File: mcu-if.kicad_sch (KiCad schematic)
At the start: 46 parts, among them J501 MCU_USB, J502 SD_Card, J503 CONN_DISP, J504 RJ45_Amphenol_RJMG1BD3B8K1ANR, SW501 BTN0, SW502 BTN1, SW503 BTN2, SW504 BTN3, U501 KSZ8081RNA

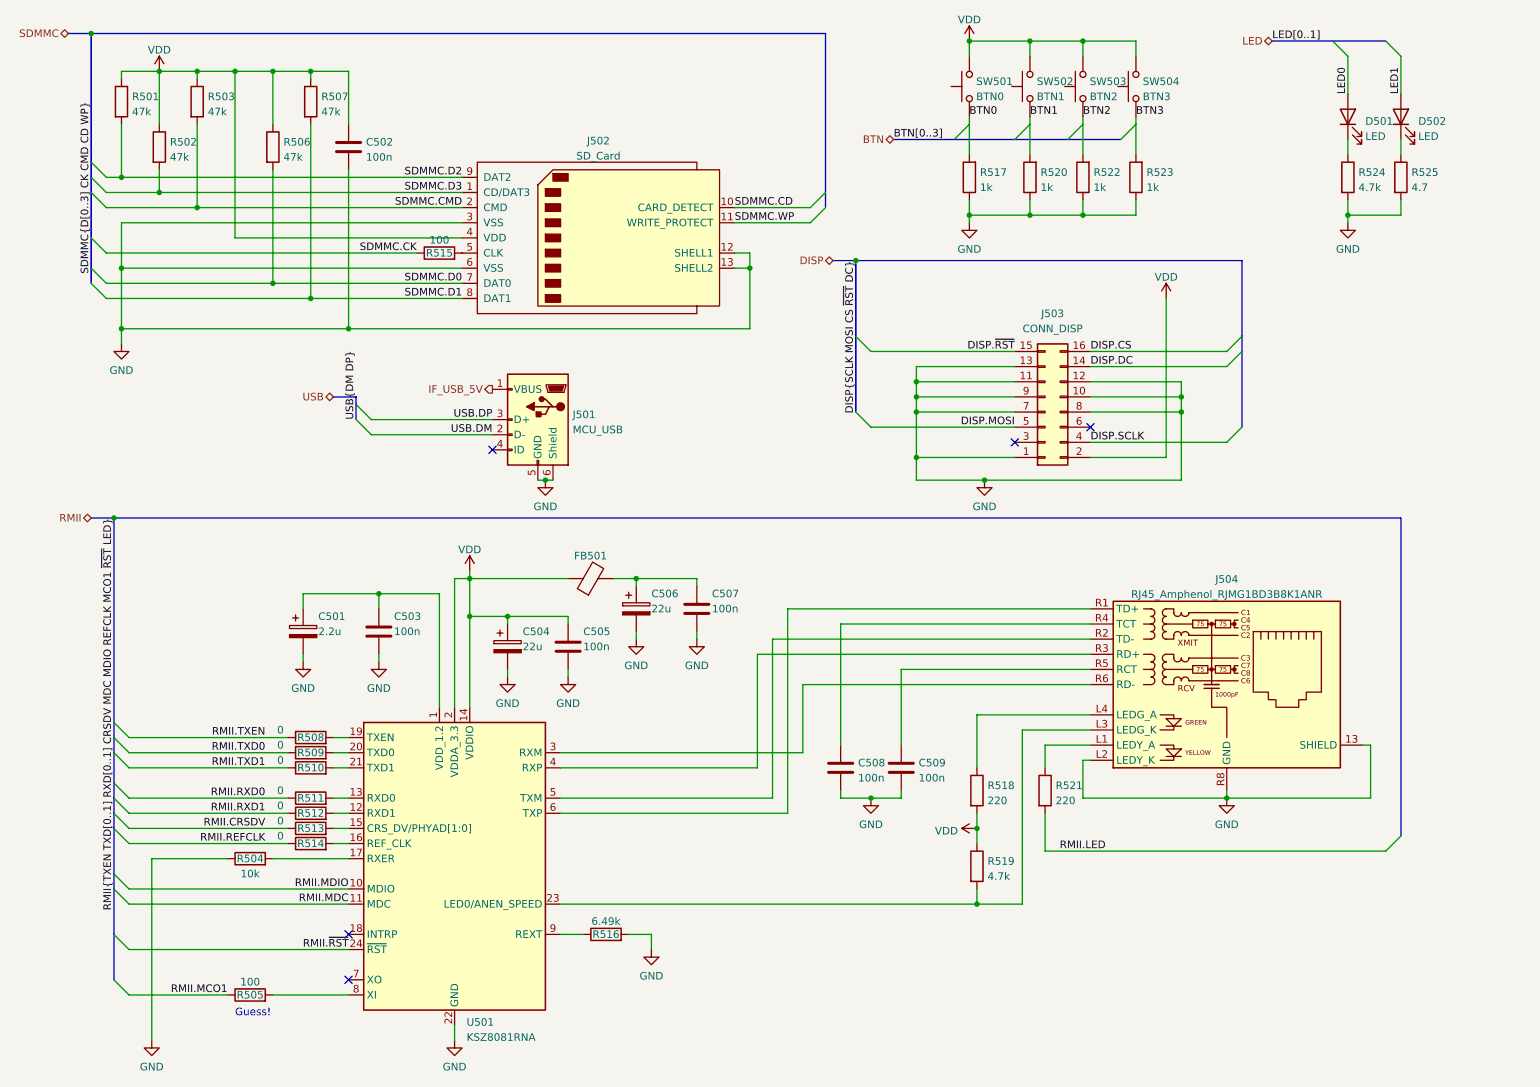
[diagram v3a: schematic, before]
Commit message: Also connect MCU USB VBUS and ID.
Useful for detecting disconnections.
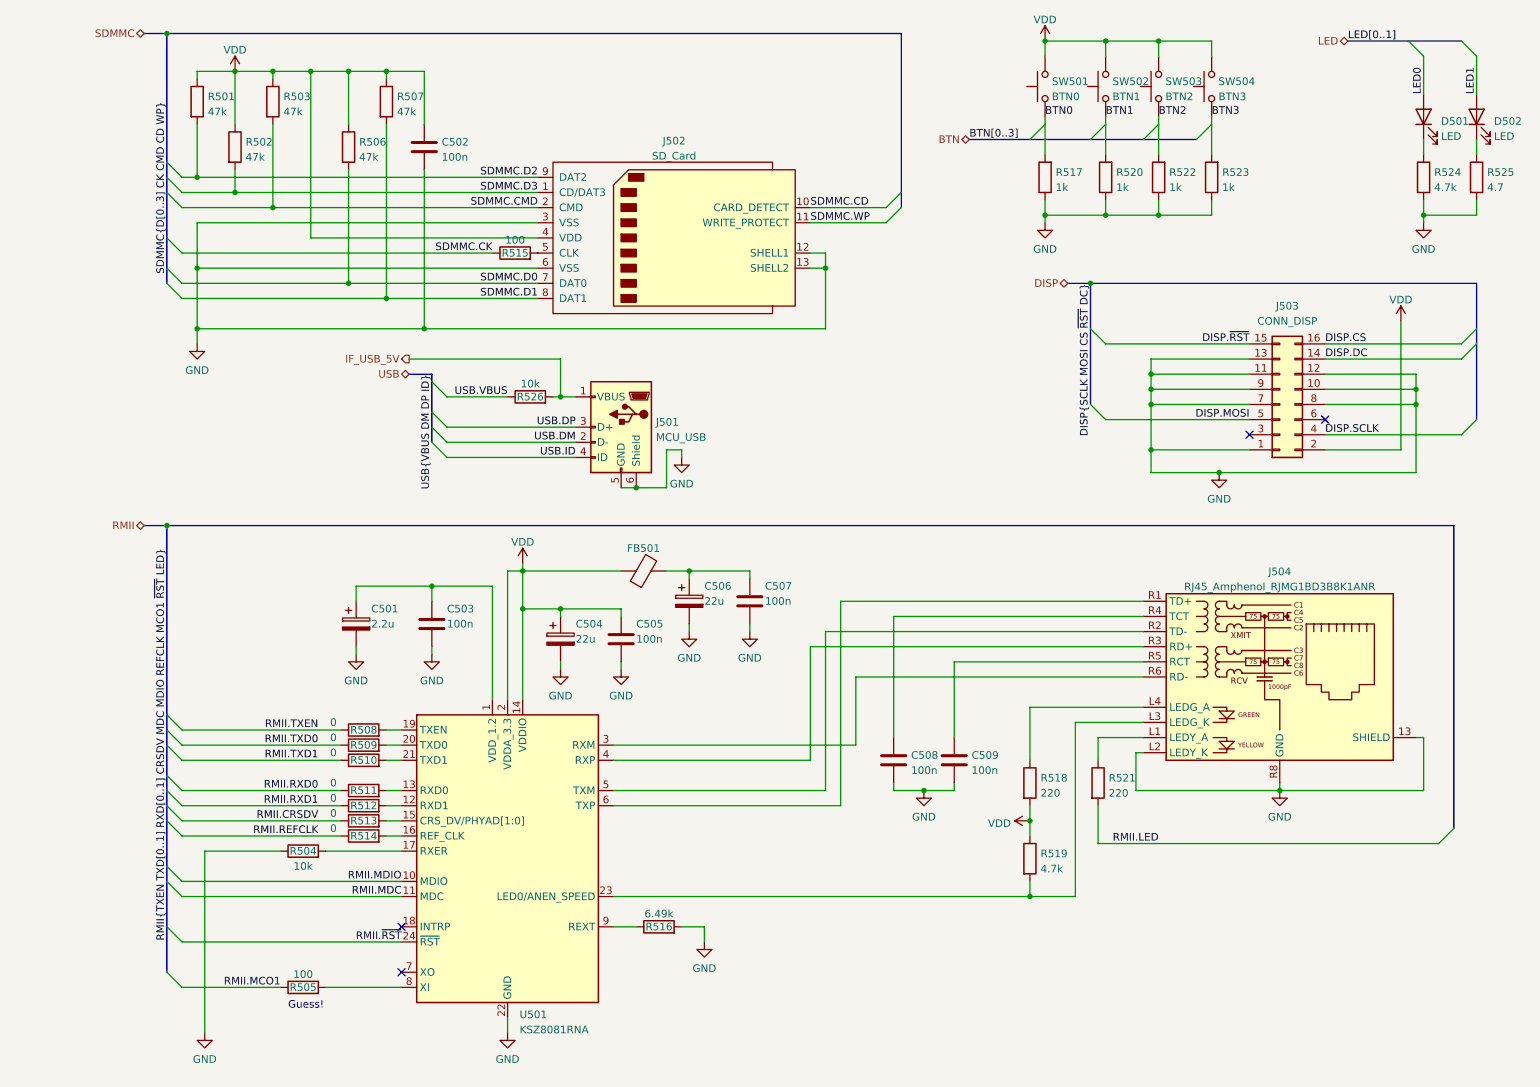
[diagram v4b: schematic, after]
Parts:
- added R526: 10k, symbol Device:R
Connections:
- net IF_USB_5V: now also R526.2
- net USB.ID: now reaches J501.4 (ID)
- new net USB.VBUS: R526.1
- no-connect marks 5 -> 4
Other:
- moved on the sheet: C501, C502, C503, C504, C505, C506, C507, C508, C509, D501, D502, FB501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

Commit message: Move programming USART to USART3 from USART1 because the pins configured by the bootloader on USART1 are now occupied.
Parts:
- R526: footprint (none) -> Resistor_SMD:R_0603_1608Metric_Pad0.98x0.95mm_HandSolder
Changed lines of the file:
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@@
     (property "Reference" "R526" (id 0) (at 101.6 80.01 90))
     (property "Value" "10k" (id 1) (at 101.6 77.8311 90))
-    (property "Footprint" "" (id 2) (at 101.6 81.788 90)
+    (property "Footprint" "Resistor_SMD:R_0603_1608Metric_Pad0.98x0.95mm_HandSolder" (id 2) (at 101.6 81.788 90)
       (effects (font (size 1.27 1.27)) hide)
     )

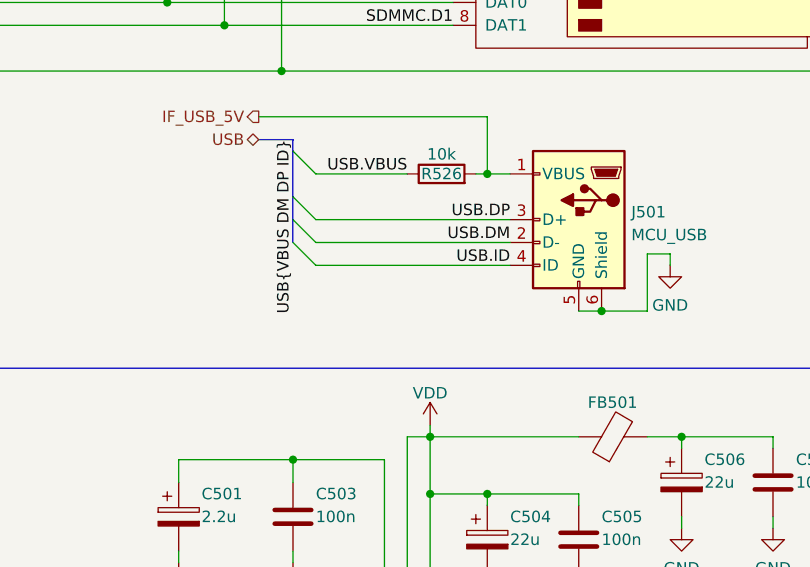
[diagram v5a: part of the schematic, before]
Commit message: Disconnect USB ID pin by default, add a solder bridge to allow reconnecting if needed.
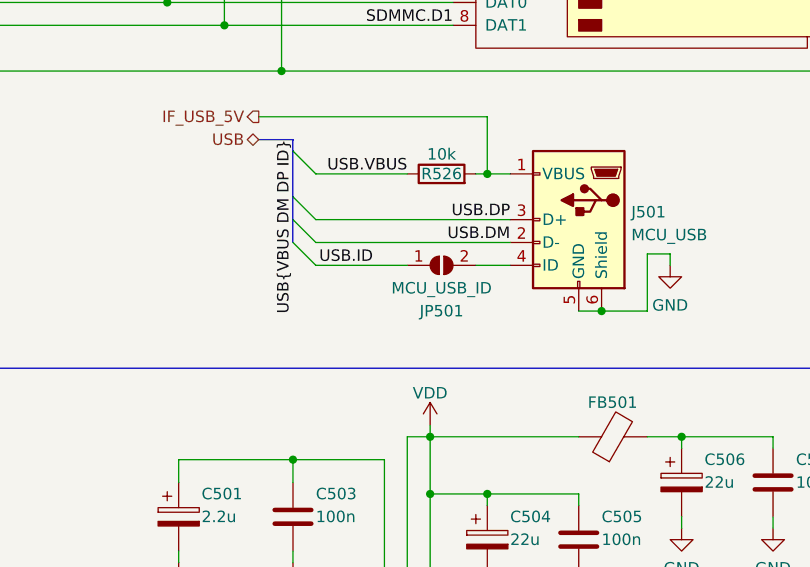
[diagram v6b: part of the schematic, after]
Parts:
- added JP501: MCU_USB_ID, Jumper:SolderJumper-2_P1.3mm_Open_RoundedPad1.0x1.5mm, symbol Jumper:SolderJumper_2_Open
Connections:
- net USB.ID: now also JP501.1 (A); no longer J501.4 (ID)
- new net: J501.4 (ID), JP501.2 (B)
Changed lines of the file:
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@@
+    (stroke (width 0) (type default) (color 0 0 0 0))
+  )
+  (wire (pts (xy 105.41 90.17) (xy 109.22 90.17))
     (stroke (width 0) (type default) (color 0 0 0 0))
   )
@@
     (stroke (width 0) (type default) (color 0 0 0 0))
   )
-  (wire (pts (xy 87.63 90.17) (xy 109.22 90.17))
-    (stroke (width 0) (type default) (color 0 0 0 0))
-  )
   (bus (pts (xy 40.64 146.05) (xy 40.64 148.59))
     (stroke (width 0) (type default) (color 0 0 0 0))
@@
     (stroke (width 0) (type default) (color 0 0 0 0))
   )
+  (wire (pts (xy 87.63 90.17) (xy 97.79 90.17))
+    (stroke (width 0) (type default) (color 0 0 0 0))
+  )
   (wire (pts (xy 77.47 148.59) (xy 80.01 148.59))
     (stroke (width 0) (type default) (color 0 0 0 0))
@@
     (effects (font (size 1.27 1.27)) (justify right bottom))
   )
-  (label "USB.ID" (at 109.22 90.17 180)
+  (label "USB.ID" (at 93.98 90.17 180)
     (effects (font (size 1.27 1.27)) (justify right bottom))
   )
@@
       (effects (font (size 1.27 1.27)) hide)
     )
+    (pin "1")
+    (pin "2")
+  )
+  (symbol (lib_id "Jumper:SolderJumper_2_Open") (at 101.6 90.17 0) (unit 1)
+    (in_bom yes) (on_board yes)
+    (property "Reference" "JP501" (id 0) (at 101.6 95.25 0))
+    (property "Value" "MCU_USB_ID" (id 1) (at 101.6 92.71 0))
+    (property "Footprint" "Jumper:SolderJumper-2_P1.3mm_Open_RoundedPad1.0x1.5mm" (id 2) (at 101.6 90.17 0)
+      (effects (font (size 1.27 1.27)) hide)
+    )
+    (property "Datasheet" "~" (id 3) (at 101.6 90.17 0)
+      (effects (font (size 1.27 1.27)) hide)
+    )

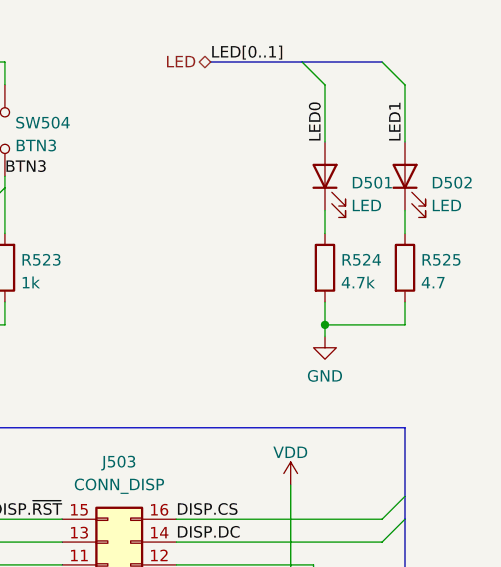
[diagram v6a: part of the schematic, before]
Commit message: Fix led current limiting resistor values.
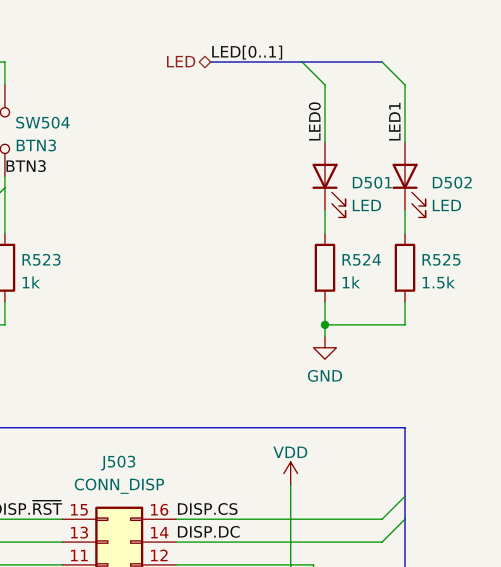
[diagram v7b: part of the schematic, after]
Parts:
- R524: value 4.7k -> 1k
- R525: value 4.7 -> 1.5k
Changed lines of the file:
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@@
       (effects (font (size 1.27 1.27)) (justify left))
     )
-    (property "Value" "4.7" (id 1) (at 262.128 44.8822 0)
+    (property "Value" "1.5k" (id 1) (at 262.128 44.8822 0)
       (effects (font (size 1.27 1.27)) (justify left))
     )
@@
       (effects (font (size 1.27 1.27)) (justify left))
     )
-    (property "Value" "4.7k" (id 1) (at 253.238 44.8822 0)
-      (effects (font (size 1.27 1.27)) (justify left))
-    )
+    (property "Value" "1k" (id 1) (at 253.238 44.8822 0)
+      (effects (font (size 1.27 1.27)) (justify left))
+    )

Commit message: Placement almost complete
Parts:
- added H501, H502: MountingHole, MountingHole:MountingHole_2.7mm_M2.5, symbol Mechanical:MountingHole
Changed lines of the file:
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@@
     (pin "2")
+  )
+  (symbol (lib_id "Mechanical:MountingHole") (at 173.99 81.28 0) (unit 1)
+    (in_bom yes) (on_board yes) (fields_autoplaced)
+    (property "Reference" "H502" (id 0) (at 176.53 80.0099 0)
+      (effects (font (size 1.27 1.27)) (justify left))
+    )
+    (property "Value" "MountingHole" (id 1) (at 176.53 82.5499 0)
+      (effects (font (size 1.27 1.27)) (justify left))
+    )
+    (property "Footprint" "MountingHole:MountingHole_2.7mm_M2.5" (id 2) (at 173.99 81.28 0)
+      (effects (font (size 1.27 1.27)) hide)
+    )
+    (property "Datasheet" "~" (id 3) (at 173.99 81.28 0)
+      (effects (font (size 1.27 1.27)) hide)
+    )
   )
   (symbol (lib_id "Device:R") (at 73.66 140.97 90) (unit 1)
@@
     (pin "2")
   )
+  (symbol (lib_id "Mechanical:MountingHole") (at 173.99 74.93 0) (unit 1)
+    (in_bom yes) (on_board yes) (fields_autoplaced)
+    (property "Reference" "H501" (id 0) (at 176.53 73.6599 0)
+      (effects (font (size 1.27 1.27)) (justify left))
+    )
+    (property "Value" "MountingHole" (id 1) (at 176.53 76.1999 0)
+      (effects (font (size 1.27 1.27)) (justify left))
+    )
+    (property "Footprint" "MountingHole:MountingHole_2.7mm_M2.5" (id 2) (at 173.99 74.93 0)
+      (effects (font (size 1.27 1.27)) hide)
+    )
+    (property "Datasheet" "~" (id 3) (at 173.99 74.93 0)
+      (effects (font (size 1.27 1.27)) hide)
+    )
+  )
   (symbol (lib_id "Device:R") (at 207.01 43.18 180) (unit 1)
